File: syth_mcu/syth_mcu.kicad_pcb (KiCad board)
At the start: 2 copper layers, 154 x 100 mm, 96 parts, among them J1 Conn_01x05, J10 Conn_01x20, J11 Conn_01x20, J2 Conn_01x05, J4 AudioPlug3, J5 Conn_01x20, J6 Conn_01x20, J7 Conn_01x16, J8 Conn_01x08, Q1 SI2307DS, Q2 SI2304DS, Q3 SI2307DS, Q4 SI2304DS, SW1 SW_Push, SW2 SW_Push, SW3 SW_Push, SW4 SW_Push, SW5 SW_Push, SW6 SW_Push, SW7 SW_SPST, U3 AMS1117-3.3, U4 AMS1117-3.3, U5 TFT_320x240

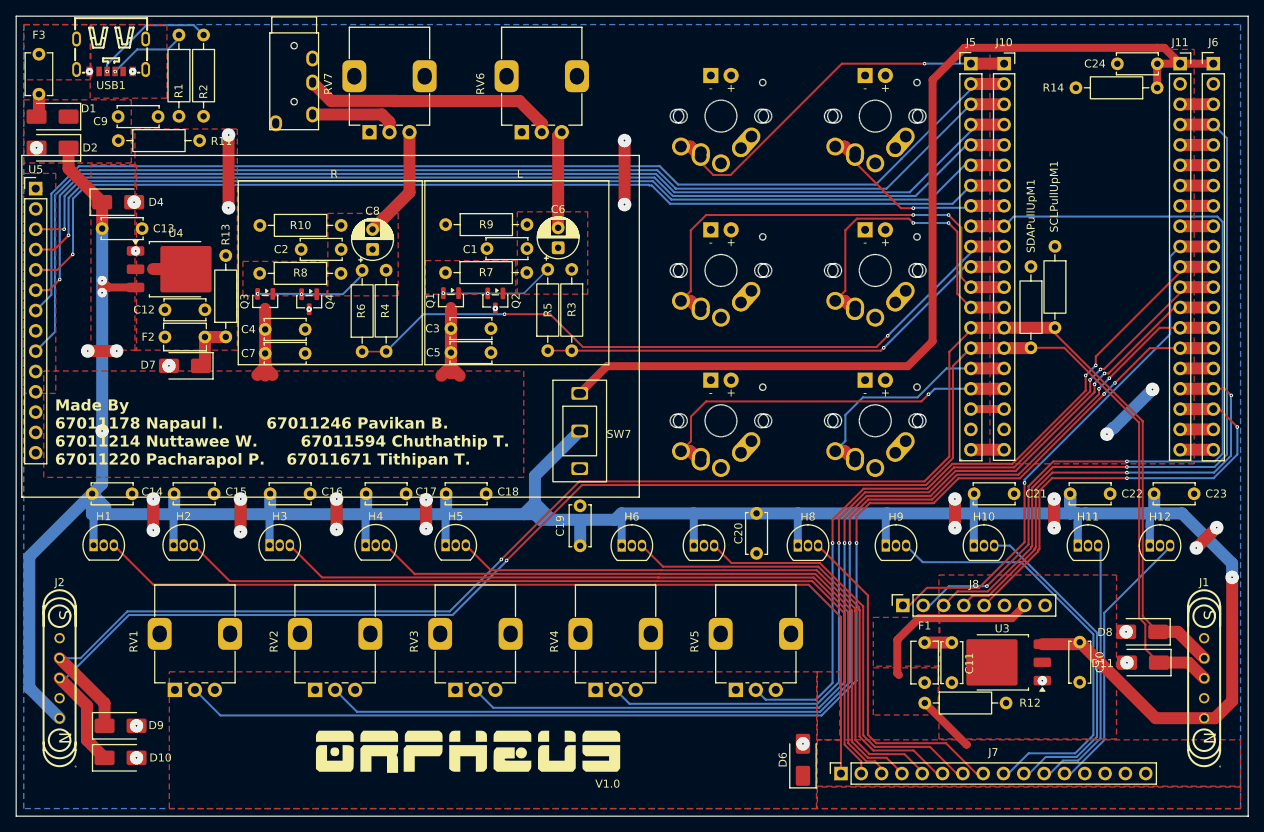
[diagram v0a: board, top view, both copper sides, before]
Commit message: pcb: fix zone priority conflicts, remove PB7 micro-stubs
- AMS1_3.3V: 5 overlapping F.Cu zones -> unique priorities 1-5
- AMS2_3.3V, Net-(U3-VO), Net-(U4-VO): second zones -> priority 2
- Net-(F3-Pad1): second zone -> priority 1
- Remove 2 PB7 sub-mm dangling stubs on B.Cu
- zones_intersect: 9 -> 0
- Remaining: PB7 F.Cu segments still need via to B.Cu (manual KiCad fix)

Claude-Session: https://claude.ai/code/session_01PBtLJ7ErrofHF5mEWAYb4x
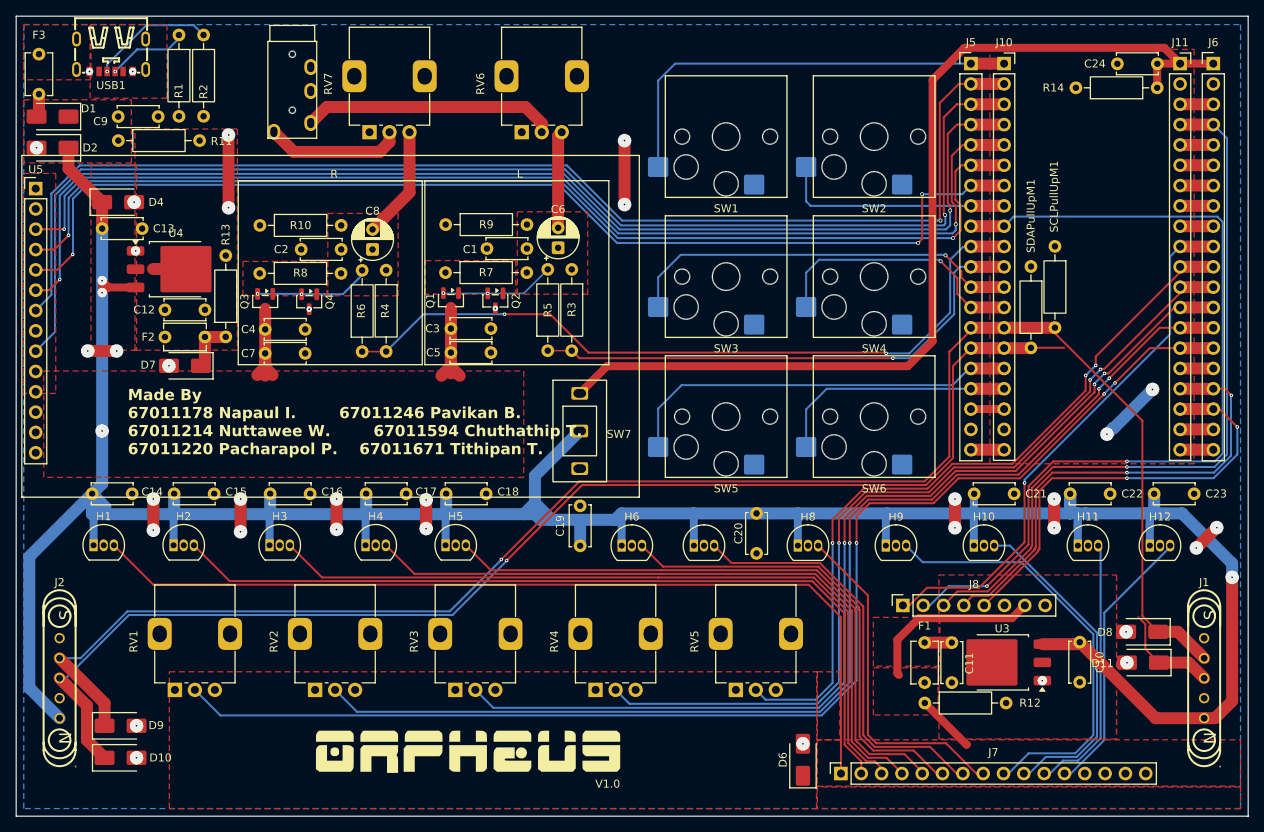
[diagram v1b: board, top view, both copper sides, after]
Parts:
- removed J4: AudioPlug3, synth:TRRS-PJ-320A
- added J3: PJ-320A, synth:TRRS-PJ-320A, F.Cu at (85.8, 50.7)
- SW1, SW2, SW3, SW4, SW5, SW6: footprint synth:MX-Alps-Choc-1U -> Switch_Keyboard_Hotswap_Kailh:SW_Hotswap_Kailh_Choc_V1_1.00u
- moved SW6 19.2 mm to (158.5, 97.6)
- moved SW5 18.6 mm to (140.0, 97.6)
- moved SW1 2.64 mm to (140.0, 62.6)
- moved SW2 2.56 mm to (158.5, 62.6)
- moved SW3 1.00 mm to (140.0, 80.1)
- moved SW4 0.78 mm to (158.5, 80.1)
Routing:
- net PB7: track 214.3 -> 175.0 mm
- net PB8: track 30.3 -> 50.1 mm
- net PB9: track 48.4 -> 30.5 mm, vias 1 -> 0
- net PB13: track 142.5 -> 155.3 mm, vias 0 -> 1
- net PB14: track 145.8 -> 157.7 mm, vias 0 -> 1
- net PA8: track 129.7 -> 140.3 mm, vias 1 -> 2
- net PB15: track 138.1 -> 148.6 mm, vias 1 -> 2
- net PA9: track 130.1 -> 140.1 mm, vias 1 -> 2
- net PB4: track 59.7 -> 50.3 mm, vias 2 -> 1
- net PB5: track 41.9 -> 33.3 mm, vias 2 -> 1
- net PA10: track 131.5 -> 138.8 mm, vias 1 -> 3
- net PB12: track 48.5 -> 54.9 mm, vias 1 -> 0
- net /DAC Channel/AudOutLeft: track 11.3 -> 17.2 mm
- net PA11: track 24.8 -> 29.6 mm, vias 1 -> 0
- net PA15: track 89.5 -> 93.6 mm
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
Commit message: pcb: cream bun review fixes (J7 position, Sim.Pins, reformat)
- J7 (1x16 MUX channel socket) moved -2.54mm in x: 154.35->151.81
  (aligns mux channels to hall sensor row)
- dac-pchannel: Sim.Pins corrected on Q1-Q4 + embedded lib defs
  SI2307DS/SI2304DS actual SOT-23 pinout: 1=G 2=S 3=D
  (was 1=D 2=G 3=S per Simulation_SPICE symbol default)
  NOTE: Sim.Pins is SPICE/documentation only — PCB pads still
  routed wrong. Full fix requires schematic symbol swap +
  PCB re-route (GUI work, see open items)
- PB7 I2C trace gap NOT fixed here — requires GUI routing
  (F.Cu gap at bbox 182.26,122.67 -> 191.53,130.30)
- Remaining changes: KiCad auto-reformat from last GUI open

Claude-Session: https://claude.ai/code/session_01VrAYoAfZXAEYgerctdkqLT
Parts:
- moved J7 2.54 mm to (151.8, 142.2)
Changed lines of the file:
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@@
 			)
 		)
+		(model "${KIPRJMOD}/local_3dmodels/Kailh_Choc.3dshapes/Kailh_LP_Choc.step"
+			(offset
+				(xyz 0 0 2.5)
+			)
+			(scale
+				(xyz 1 1 1)
+			)
+			(rotate
+				(xyz -90 -0 -90)
+			)
+		)
 	)
 	(footprint "LOGO"
@@
 			)
 			(rotate
-				(xyz 0 0 0)
+				(xyz -0 -0 -0)
+			)
+		)
+		(model "${KIPRJMOD}/local_3dmodels/Kailh_Choc.3dshapes/Kailh_LP_Choc.step"
+			(offset
+				(xyz 0 0 2.5)
+			)
+			(scale
+				(xyz 1 1 1)
+			)
+			(rotate
+				(xyz -90 -0 -90)
 			)
 		)
@@
 	(footprint "Connector_PinSocket_2.54mm:PinSocket_1x16_P2.54mm_Vertical"
 		(layer "F.Cu")
-		(at 154.35 142.2175 90)
+		(at 151.81 142.2175 90)
 		(descr "Through hole straight socket strip, 1x16, 2.54mm pitch, single row (from Kicad 4.0.7), script generated")
 		(tags "Through hole socket strip THT 1x16 2.54mm single row")
@@
 			)
 			(rotate
-				(xyz 0 0 0)
+				(xyz -0 -0 -0)
+			)
+		)
+		(model "${KIPRJMOD}/local_3dmodels/Kailh_Choc.3dshapes/Kailh_LP_Choc.step"
+			(offset
+				(xyz 0 0 2.5)
+			)
+			(scale
+				(xyz 1 1 1)
+			)
+			(rotate
+				(xyz -90 -0 -90)
 			)
 		)
@@
 			)
 		)
+		(model "${KIPRJMOD}/local_3dmodels/Kailh_Choc.3dshapes/Kailh_LP_Choc.step"
+			(offset
+				(xyz 0 0 2.5)
+			)
+			(scale
+				(xyz 1 1 1)
+			)
+			(rotate
+				(xyz -90 -0 -90)
+			)
+		)
 	)
 	(footprint "Capacitor_THT:C_Disc_D5.0mm_W2.5mm_P5.00mm"
@@
 			)
 		)
+		(model "${KIPRJMOD}/local_3dmodels/Kailh_Choc.3dshapes/Kailh_LP_Choc.step"
+			(offset
+				(xyz 0 0 2.5)
+			)
+			(scale
+				(xyz 1 1 1)
+			)
+			(rotate
+				(xyz -90 -0 -90)
+			)
+		)
 	)
 	(footprint "Package_TO_SOT_THT:TO-92_Inline"
@@
 			)
 		)
+		(model "${KIPRJMOD}/local_3dmodels/Kailh_Choc.3dshapes/Kailh_LP_Choc.step"
+			(offset
+				(xyz 0 0 2.5)
+			)
+			(scale
+				(xyz 1 1 1)
+			)
+			(rotate
+				(xyz -90 -0 -90)
+			)
+		)
 	)
 	(footprint "Connector_PinSocket_2.54mm:PinSocket_1x20_P2.54mm_Vertical"
@@
 	)
 	(segment
+		(start 100.419151 69.585962)
+		(end 100.419151 62.05)
+		(width 1.5)
+		(layer "F.Cu")
+		(net "Net-(C8-Pad2)")
+	)
+	(segment
+		(start 95.8 74.205113)
+		(end 100.419151 69.585962)
+		(width 1.5)
+		(layer "F.Cu")
+		(net "Net-(C8-Pad2)")
+	)
+	(segment
 		(start 116.95 60.941672)
 		(end 116.95 62.05)
@@
 	)
 	(segment
-		(start 100.419151 69.585962)
-		(end 100.419151 62.05)
-		(width 1.5)
-		(layer "F.Cu")
-		(net "Net-(C8-Pad2)")
-	)
-	(segment
-		(start 95.8 74.205113)
-		(end 100.419151 69.585962)
-		(width 1.5)
-		(layer "F.Cu")
-		(net "Net-(C8-Pad2)")
-	)
-	(segment

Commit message: fix trace gap
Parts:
- moved D6 4.11 mm to (145.5, 140.5)
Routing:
- net PB7: track 175.0 -> 212.5 mm
- net C10: track 33.3 -> 37.3 mm
- net C11: track 34.7 -> 38.6 mm
- net C9: track 41.6 -> 45.6 mm
- net C8: track 54.0 -> 57.5 mm
- net C4: track 78.6 -> 76.0 mm
- net C7: track 42.7 -> 40.3 mm
- net C5: track 58.8 -> 56.5 mm
- net C6: track 52.3 -> 50.5 mm
- net C3: track 86.0 -> 84.4 mm
- net C1: track 106.0 -> 104.8 mm
- net C2: track 95.8 -> 94.6 mm
- net C0: track 114.2 -> 113.1 mm
- net C12: track 0.00 -> 0.79 mm

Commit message: Fixes from review 2
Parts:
- F1, F2: footprint Capacitor_THT:C_Disc_D5.1mm_W3.2mm_P5.00mm -> synth:RXEF040
- F3: footprint Capacitor_THT:C_Disc_D5.1mm_W3.2mm_P5.00mm -> synth:RXEF160
- Q1, Q2, Q3, Q4: footprint Package_TO_SOT_SMD:SOT-23 -> synth:SI230x SOT-23
- U5: footprint Connector_PinHeader_2.54mm:PinHeader_1x14_P2.54mm_Vertical -> Connector_PinSocket_2.54mm:PinSocket_1x14_P2.54mm_Vertical
- moved D2 6.00 mm to (60.6, 60.4), turned to 90 degrees
- moved USB1 4.68 mm to (67.8, 52.4)
- moved R1 4.43 mm to (76.0, 49.7)
- moved R2 4.43 mm to (79.1, 49.7)
- moved C9 4.40 mm to (68.4, 60.1)
- moved R11 3.58 mm to (67.6, 63.1)
- moved F3 3.52 mm to (53.2, 55.7)
- moved F1 2.78 mm to (165.2, 128.6)
- moved C2 1.50 mm to (91.9, 75.2)
- moved C8 1.50 mm to (95.8, 75.2)
- moved R10 1.50 mm to (81.7, 72.2)
- moved R8 1.50 mm to (81.7, 78.2)
- moved C1 1.43 mm to (115.1, 75.2)
- moved R7 1.43 mm to (104.9, 78.2)
- moved R9 1.43 mm to (104.9, 72.2)
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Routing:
- net D_5V: track 374.4 -> 510.9 mm, vias 4 -> 3
- net GND: track 54.8 -> 104.1 mm, vias 36 -> 42
- net PA12: track 110.8 -> 91.4 mm, vias 2 -> 5
- net PC14: track 55.3 -> 47.3 mm, vias 2 -> 1
- net PB10: track 94.5 -> 87.5 mm, vias 1 -> 4
- net PC15: track 59.9 -> 53.0 mm, vias 2 -> 1
- net AMS2_3.3V: track 32.5 -> 25.8 mm
- net AMS1_3.3V: track 29.6 -> 35.4 mm
- net 3V3: track 8.31 -> 13.8 mm, vias 0 -> 1
- net Net-(Q1-G): track 14.3 -> 17.4 mm
- net Net-(Q3-G): track 14.7 -> 17.0 mm
- net Net-(U4-VO): track 3.97 -> 6.16 mm
- net Net-(C8-Pad2): track 14.1 -> 12.6 mm
- net Net-(C6-Pad2): track 12.1 -> 10.7 mm
- net PA3: track 110.3 -> 111.7 mm
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- removed copper zone on F.Cu, net D_5V

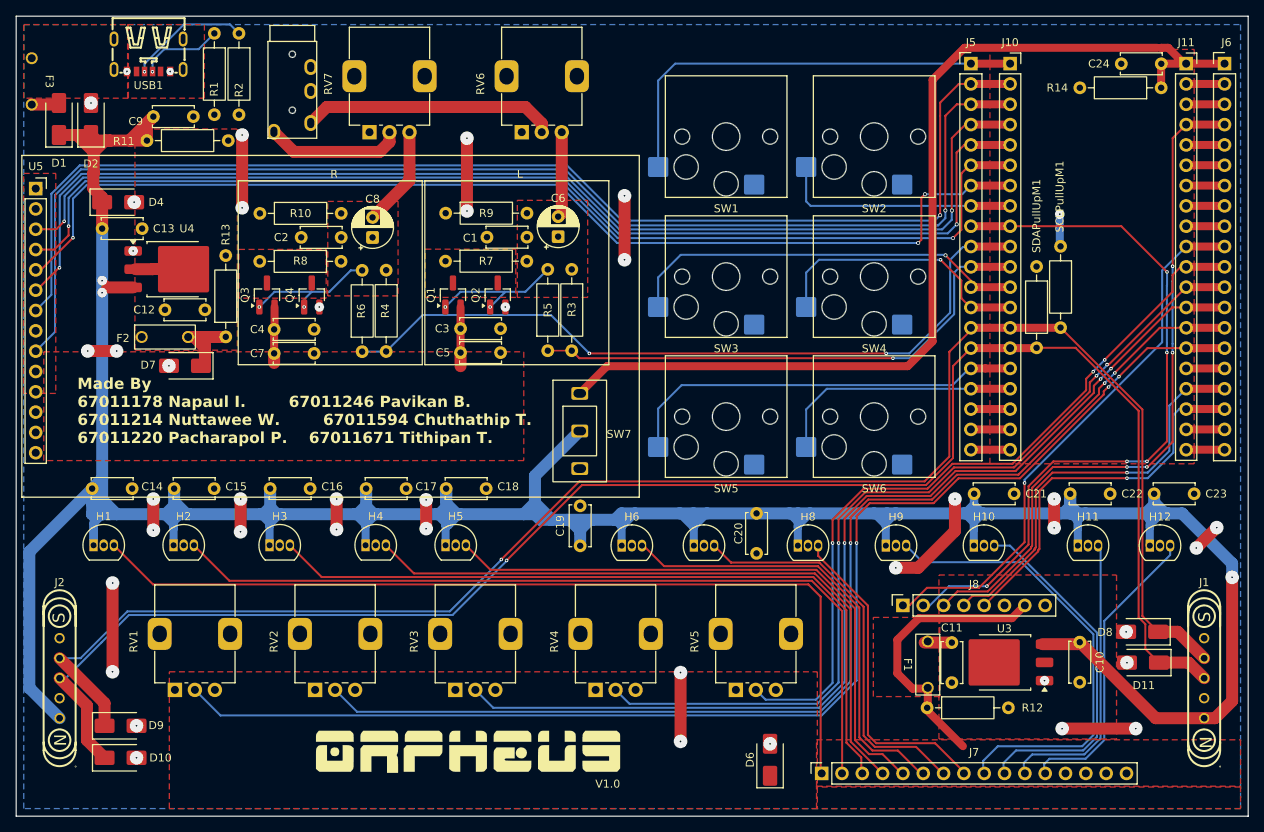
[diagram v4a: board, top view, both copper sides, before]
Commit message: add screw hole
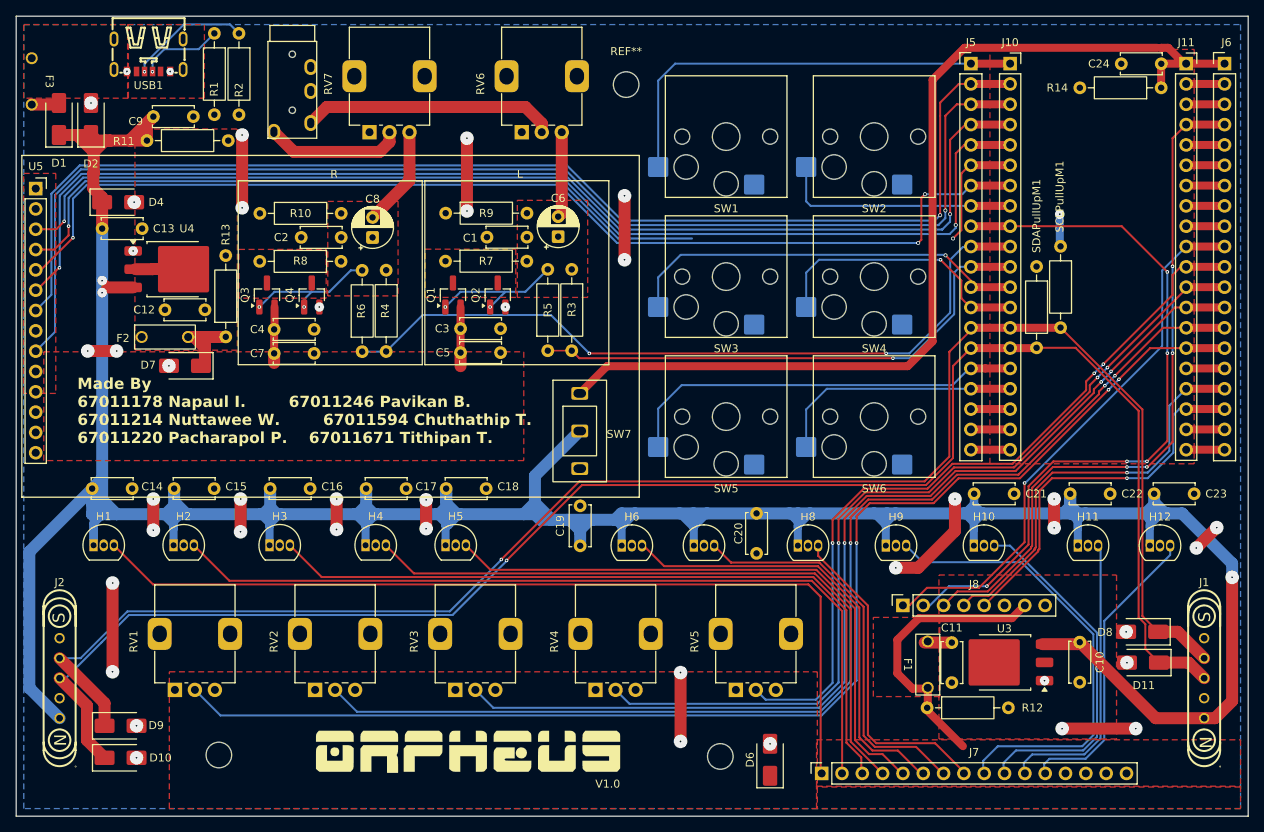
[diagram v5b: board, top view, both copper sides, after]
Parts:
- added REF**: MountingHole_3.2mm_M3, MountingHole:MountingHole_3.2mm_M3, F.Cu at (127.5, 56.1)
- added REF**: MountingHole_3.2mm_M3, MountingHole:MountingHole_3.2mm_M3, F.Cu at (76.6, 139.9)
- added REF**: MountingHole_3.2mm_M3, MountingHole:MountingHole_3.2mm_M3, F.Cu at (139.3, 140.1)
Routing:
- net PA9: track 138.9 -> 106.4 mm
